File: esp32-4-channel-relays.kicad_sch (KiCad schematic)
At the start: 27 parts, among them Q1 MBT3904DW1, SW1 SW_SKQG, SW2 SW_SKQG, U1 AMS1117-3.3, U2 CH340C, U3 PRTR5V0U2X, U4 ESP32-WROOM-32

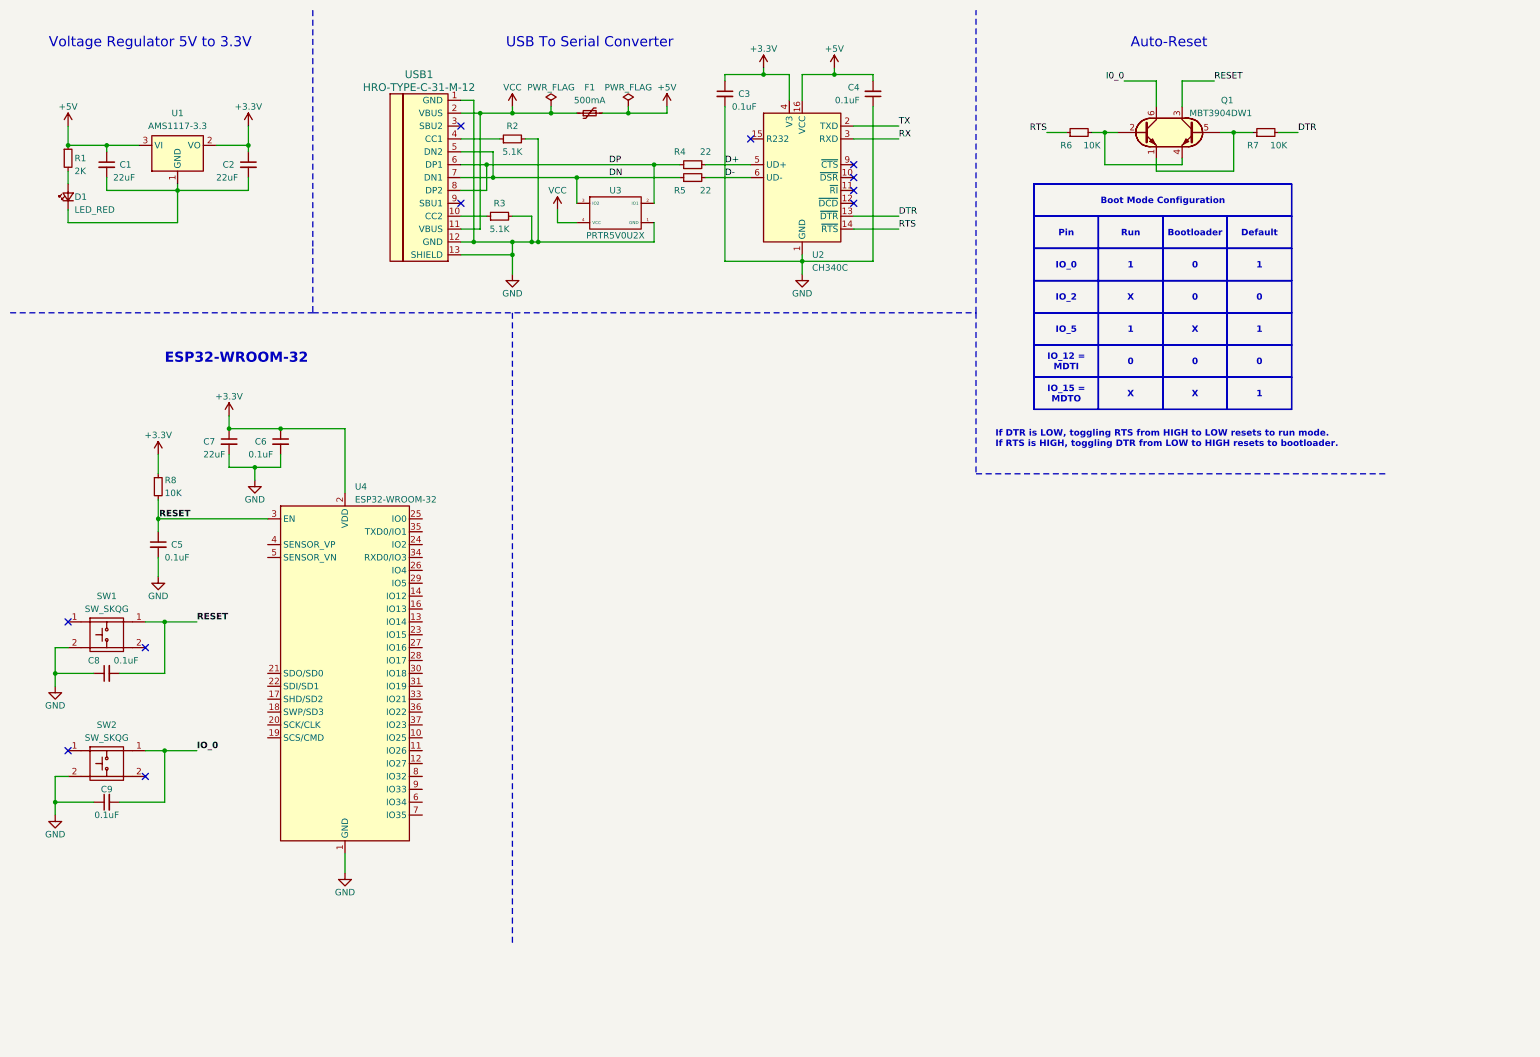
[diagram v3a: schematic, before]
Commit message: Add 4-channel relays to the schematic
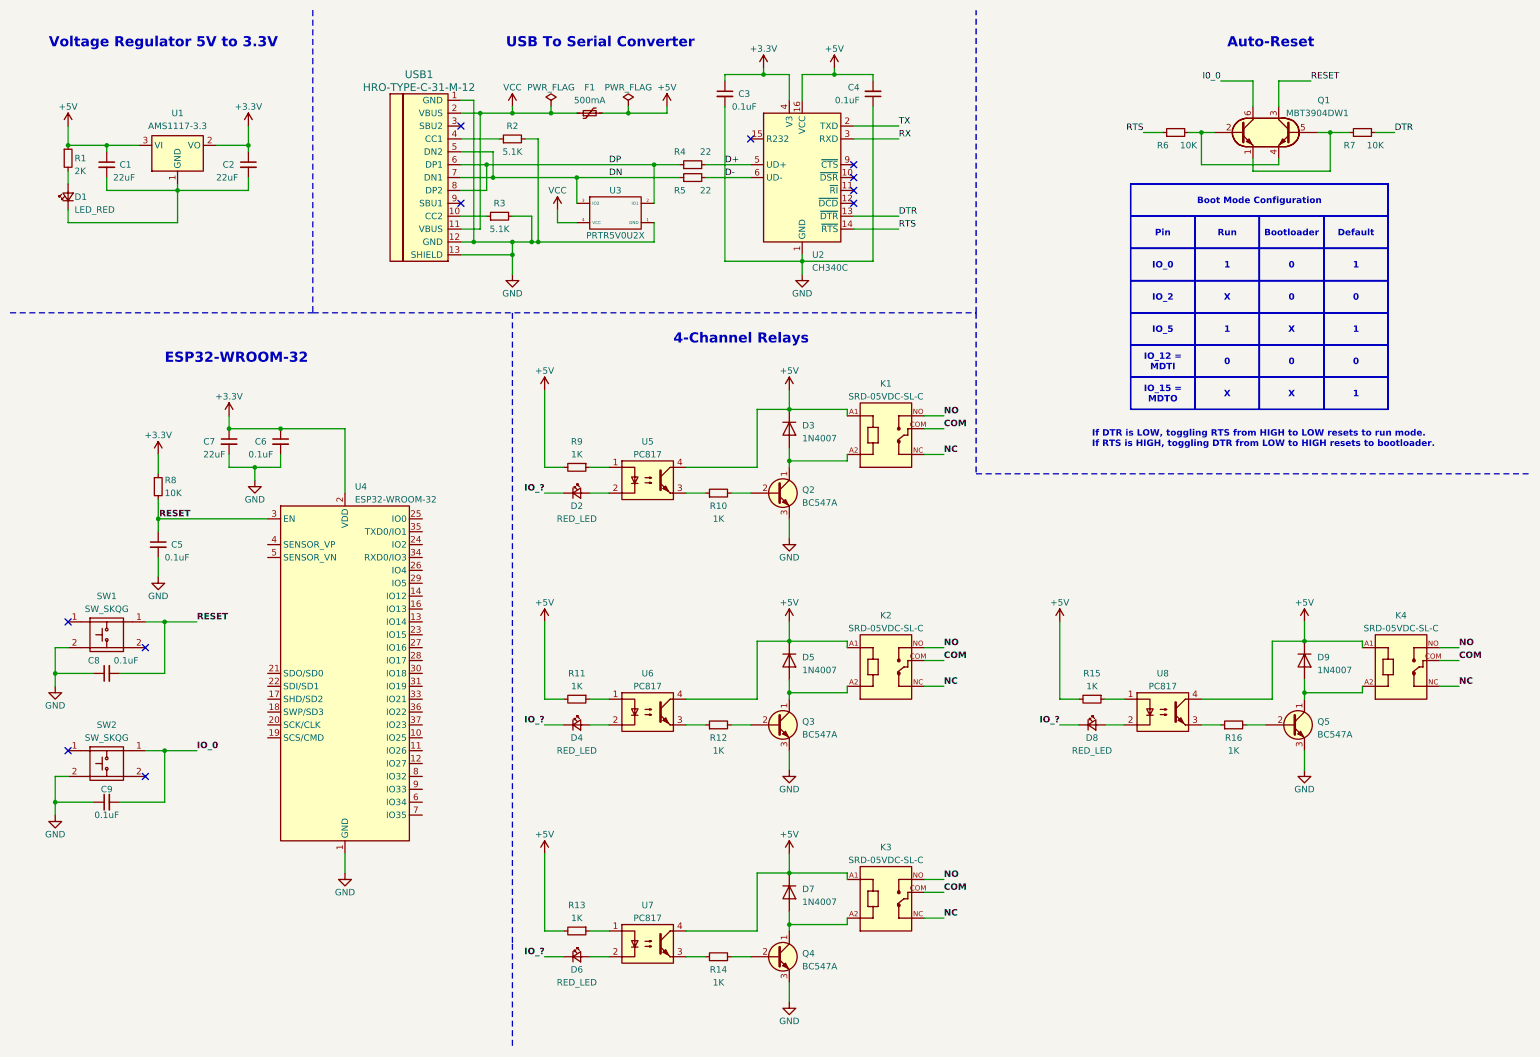
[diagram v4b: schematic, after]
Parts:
- added D2, D4, D6, D8: RED_LED, symbol Device:LED_Small
- added D3, D5, D7, D9: 1N4007, Diode_SMD:D_MELF_Handsoldering, symbol local_lib:1N4007
- added K1, K2, K3, K4: SRD-05VDC-SL-C, RELAY_SRD-05VDC-SL-C, symbol local_lib:SRD-05VDC-SL-C
- added Q2, Q3, Q4, Q5: BC547A, Package_TO_SOT_THT_AKL:TO-92_Inline_Wide_CBE, symbol local_lib:BC547A
- added R10, R11, R12, R13, R14, R15, R16, R9: 1K, symbol Device:R_Small
- added U5, U6, U7, U8: PC817, Package_DIP:DIP-4_W7.62mm, symbol local_lib:PC817
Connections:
- net +5V: now also D3.1 (K), D5.1 (K), D7.1 (K), D9.1 (K), K1.A1, K2.A1, K3.A1, K4.A1, R11.2, R13.2, R15.2, R9.2, U5.4, U6.4, U7.4, U8.4
- net GND: now also Q2.3 (E), Q3.3 (E), Q4.3 (E), Q5.3 (E)
- new net: D2.2 (A), U5.2
- new net: D4.2 (A), U6.2
- new net: R15.1, U8.1
- new net: D8.2 (A), U8.2
- new net: R16.1, U8.3
- new net: D7.2 (A), K3.A2, Q4.1 (C)
- new net: Q4.2 (B), R14.2
- new net: R13.1, U7.1
- new net: D6.2 (A), U7.2
- new net: R14.1, U7.3
- new net: R9.1, U5.1
- new net: D9.2 (A), K4.A2, Q5.1 (C)
- new net: R11.1, U6.1
- new net: D3.2 (A), K1.A2, Q2.1 (C)
- new net: Q2.2 (B), R10.2
- new net: R10.1, U5.3
- new net: Q5.2 (B), R16.2
- new net: D5.2 (A), K2.A2, Q3.1 (C)
- new net: Q3.2 (B), R12.2
- new net: R12.1, U6.3
- new net COM: K1.COM, K2.COM, K3.COM, K4.COM
- new net IO_?: D2.1 (K), D4.1 (K), D6.1 (K), D8.1 (K)
- new net NC: K1.NC, K2.NC, K3.NC, K4.NC
- new net NO: K1.NO, K2.NO, K3.NO, K4.NO
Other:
- note added: "4-Channel Relays"
- title: (none) -> ESP32 4 Channel Relays
- moved on the sheet: Q1, R6, R7

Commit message: Add screw terminal  for relay output and wiring relay input to esp32 GPIO
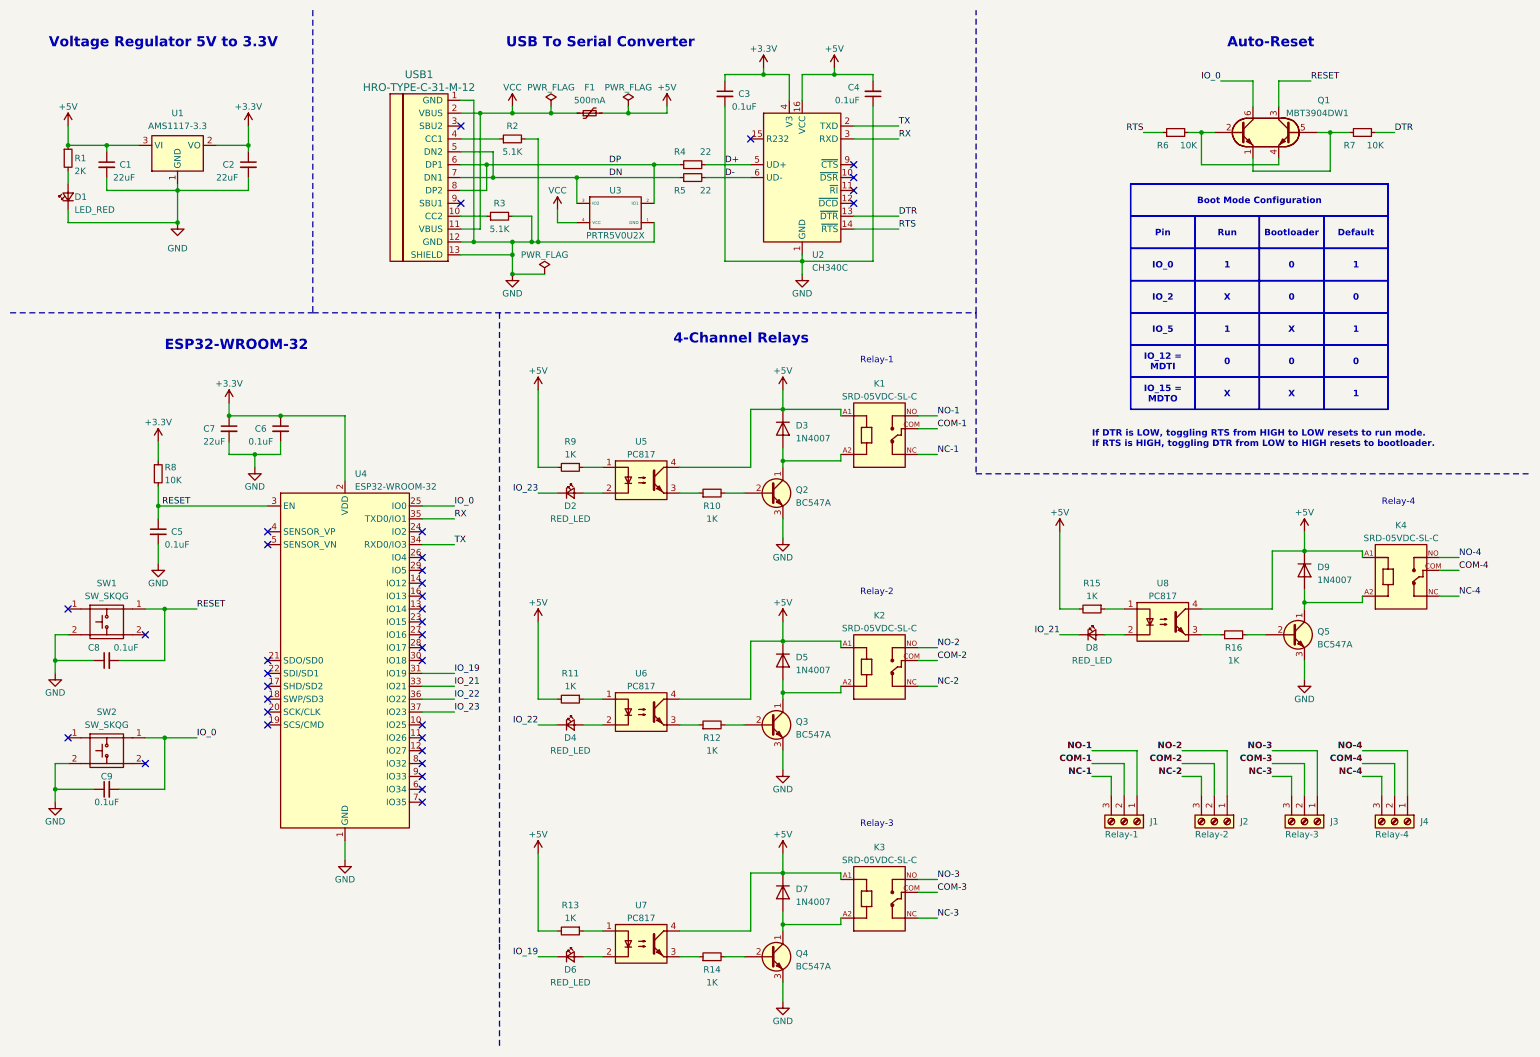
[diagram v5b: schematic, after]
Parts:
- added J1: Relay-1, symbol Connector:Screw_Terminal_01x03
- added J2: Relay-2, symbol Connector:Screw_Terminal_01x03
- added J3: Relay-3, symbol Connector:Screw_Terminal_01x03
- added J4: Relay-4, symbol Connector:Screw_Terminal_01x03
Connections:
- net I0_0 is gone; now on net IO_0: Q1.6 (C1)
- net GND: now also C1.2, C2.2, D1.1 (K), U1.1 (GND)
- net IO_0: now also U4.25 (IO0)
- net RX: now also U4.35 (TXD0/IO1)
- net TX: now also U4.34 (RXD0/IO3)
- net IO_19: now reaches U4.31 (IO19)
- net IO_19: now also D6.1 (K)
- net IO_21: now reaches U4.33 (IO21)
- net IO_21: now also D8.1 (K)
- net IO_22: now reaches U4.36 (IO22)
- net IO_22: now also D4.1 (K)
- net IO_23: now reaches U4.37 (IO23)
- net IO_23: now also D2.1 (K)
- removed net COM: K1.COM, K2.COM, K3.COM, K4.COM
- removed net IO_?: D2.1 (K), D4.1 (K), D6.1 (K), D8.1 (K)
- removed net NC: K1.NC, K2.NC, K3.NC, K4.NC
- removed net NO: K1.NO, K2.NO, K3.NO, K4.NO
- new net COM-1: J1.2 (Pin_2), K1.COM
- new net COM-2: J2.2 (Pin_2), K2.COM
- new net COM-3: J3.2 (Pin_2), K3.COM
- new net COM-4: J4.2 (Pin_2), K4.COM
- new net NC-1: J1.3 (Pin_3), K1.NC
- new net NC-2: J2.3 (Pin_3), K2.NC
- new net NC-3: J3.3 (Pin_3), K3.NC
- new net NC-4: J4.3 (Pin_3), K4.NC
- new net NO-1: J1.1 (Pin_1), K1.NO
- new net NO-2: J2.1 (Pin_1), K2.NO
- new net NO-3: J3.1 (Pin_1), K3.NO
- new net NO-4: J4.1 (Pin_1), K4.NO
- no-connect marks 11 -> 36
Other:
- note added: "Relay-1"
- note added: "Relay-2"
- note added: "Relay-3"
- note added: "Relay-4"
- moved on the sheet: C5, C6, C7, C8, C9, D2, D3, D4, D5, D6, D7, D8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

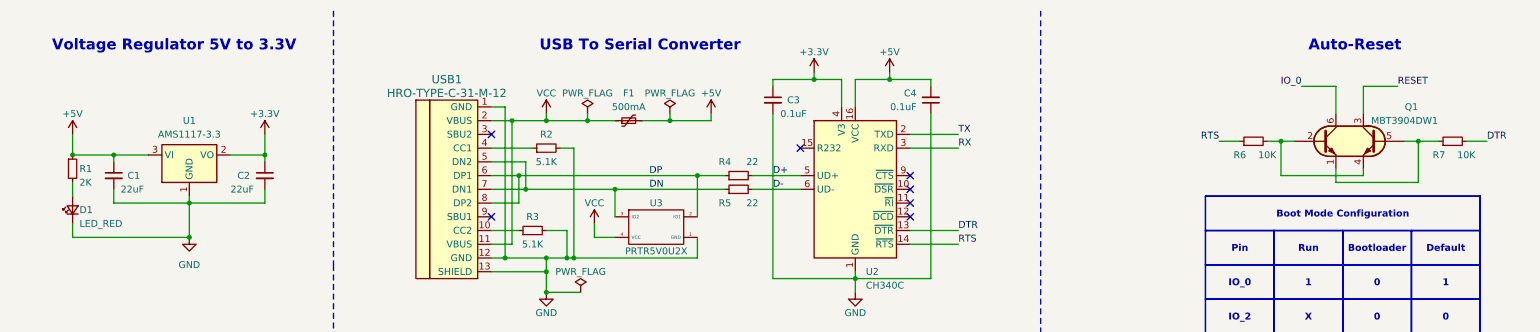
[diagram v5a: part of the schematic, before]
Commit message: Assign footprints
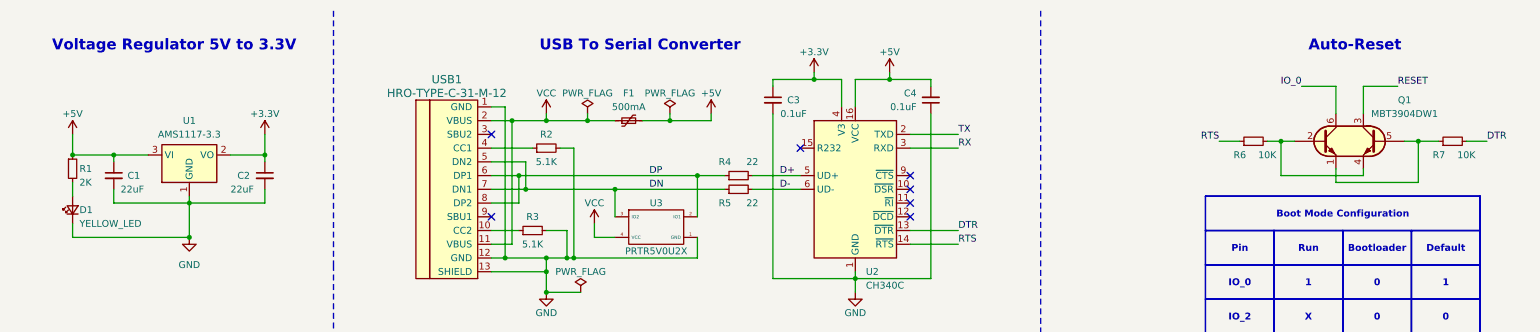
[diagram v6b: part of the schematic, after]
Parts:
- C1, C2, C3, C4, C5, C6, C7, C8, C9: footprint (none) -> Capacitor_SMD:C_0805_2012Metric_Pad1.18x1.45mm_HandSolder
- D1: value LED_RED -> YELLOW_LED; footprint (none) -> LED_SMD:LED_0805_2012Metric_Pad1.15x1.40mm_HandSolder
- D2, D4, D6, D8: footprint (none) -> LED_SMD:LED_0805_2012Metric_Pad1.15x1.40mm_HandSolder
- D3, D5, D7, D9: footprint Diode_SMD:D_MELF_Handsoldering -> local_lib:D_MELF_Handsoldering
- F1: footprint (none) -> Fuse:Fuse_1206_3216Metric_Pad1.42x1.75mm_HandSolder
- J1, J2, J3, J4: footprint (none) -> TerminalBlock_Phoenix:TerminalBlock_Phoenix_MKDS-1,5-3-5.08_1x03_P5.08mm_Horizontal
- K1, K2, K3, K4: footprint RELAY_SRD-05VDC-SL-C -> local_lib:RELAY_SRD-05VDC-SL-C
- Q1: footprint Package_TO_SOT_SMD_AKL:SOT-363_SC-70-6 -> local_lib:SOT-363_SC-70-6_Handsoldering
- Q2, Q3, Q4, Q5: footprint Package_TO_SOT_THT_AKL:TO-92_Inline_Wide_CBE -> local_lib:TSOT-23_HandSoldering
- R1, R10, R11, R12, R13, R14, R15, R16, R2, R3, R4, R5, R6, R7, R8, R9: footprint (none) -> Resistor_SMD:R_0805_2012Metric_Pad1.20x1.40mm_HandSolder
- SW1, SW2: footprint Button_Switch_SMD:SW_SPST_SKQG_WithStem -> local_lib:SW_SPST_SKQG_WithStem
- U1: footprint Package_TO_SOT_SMD:SOT-223-3_TabPin2 -> local_lib:SOT-223-3_TabPin2
- U2: footprint Package_SO:SOIC-16_3.9x9.9mm_P1.27mm -> local_lib:SOIC-16_3.9x9.9mm_P1.27mm
- U3: footprint Package_TO_SOT_SMD:SOT-143 -> local_lib:SOT-143_Handsoldering
- U4: footprint RF_Module:ESP32-WROOM-32 -> local_lib:ESP32-WROOM-32
- U5, U6, U7, U8: footprint Package_DIP:DIP-4_W7.62mm -> local_lib:SMDIP-4_W7.62mm
- USB1: footprint (none) -> local_lib:HRO-TYPE-C-31-M-12-HandSoldering
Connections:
- net GND: no longer R4.2, R5.2, U2.5 (UD+), U2.6 (UD-)
- new net D+: R4.2, U2.5 (UD+)
- new net D-: R5.2, U2.6 (UD-)

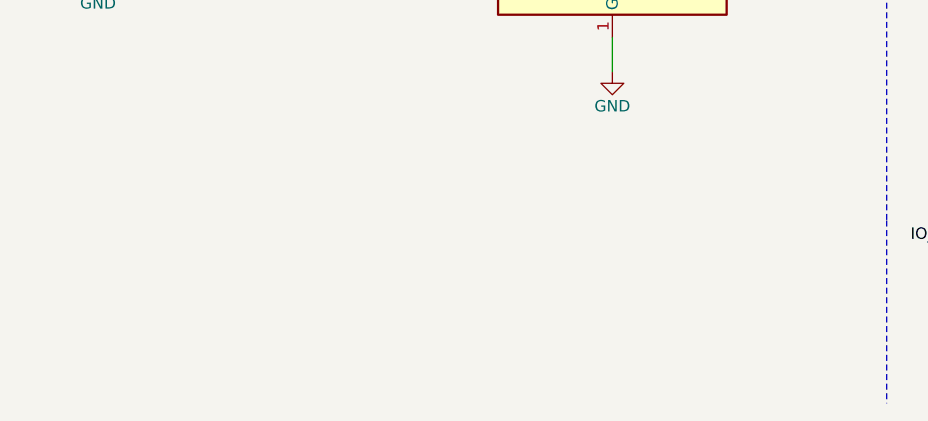
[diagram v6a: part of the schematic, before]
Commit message: Add mounting hole symbols and assign footprint
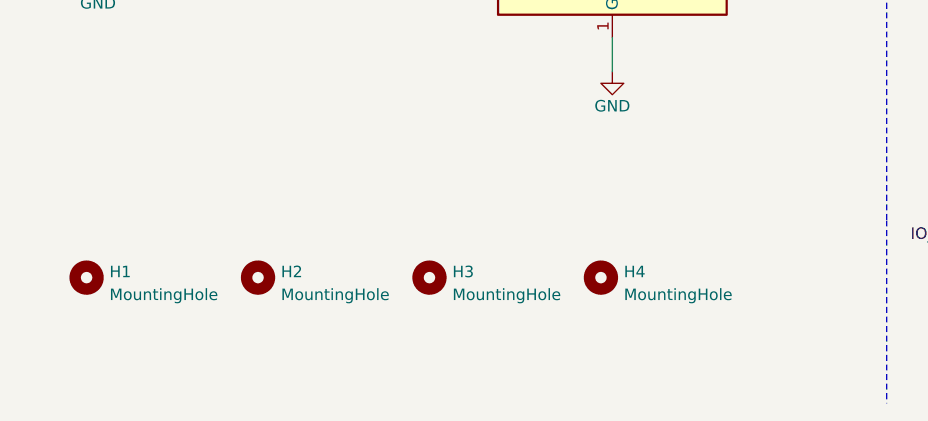
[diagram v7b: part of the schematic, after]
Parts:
- added H1, H2, H3, H4: MountingHole, MountingHole:MountingHole_3.2mm_M3, symbol Mechanical:MountingHole
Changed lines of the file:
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@@
+    )
+  )
+  (symbol (lib_id "Mechanical:MountingHole") (at 20.32 203.2 0) (unit 1)
+    (in_bom yes) (on_board yes) (dnp no) (fields_autoplaced)
+    (property "Reference" "H1" (at 22.86 202.565 0)
+      (effects (font (size 1.27 1.27)) (justify left))
+    )
+    (property "Value" "MountingHole" (at 22.86 205.105 0)
+      (effects (font (size 1.27 1.27)) (justify left))
+    )
+    (property "Footprint" "MountingHole:MountingHole_3.2mm_M3" (at 20.32 203.2 0)
+      (effects (font (size 1.27 1.27)) hide)
+    )
+    (property "Datasheet" "~" (at 20.32 203.2 0)
+      (effects (font (size 1.27 1.27)) hide)
+    )
+    (instances
+      (project "esp32-4-channel-relays"
+        (path "/8eb0840c-04b5-48e5-b6dd-a6c2b294f86f"
+          (reference "H1") (unit 1)
+        )
+      )
     )
   )
@@
     )
   )
+  (symbol (lib_id "Mechanical:MountingHole") (at 58.42 203.2 0) (unit 1)
+    (in_bom yes) (on_board yes) (dnp no) (fields_autoplaced)
+    (property "Reference" "H3" (at 60.96 202.565 0)
+      (effects (font (size 1.27 1.27)) (justify left))
+    )
+    (property "Value" "MountingHole" (at 60.96 205.105 0)
+      (effects (font (size 1.27 1.27)) (justify left))
+    )
+    (property "Footprint" "MountingHole:MountingHole_3.2mm_M3" (at 58.42 203.2 0)
+      (effects (font (size 1.27 1.27)) hide)
+    )
+    (property "Datasheet" "~" (at 58.42 203.2 0)
+      (effects (font (size 1.27 1.27)) hide)
+    )
+    (instances
+      (project "esp32-4-channel-relays"
+        (path "/8eb0840c-04b5-48e5-b6dd-a6c2b294f86f"
+          (reference "H3") (unit 1)
+        )
+      )
+    )
+  )
   (symbol (lib_id "Device:LED_Small") (at 123.19 199.39 0) (unit 1)
     (in_bom yes) (on_board yes) (dnp no)
@@
         (path "/8eb0840c-04b5-48e5-b6dd-a6c2b294f86f"
           (reference "#PWR015") (unit 1)
+        )
+      )
+    )
+  )
+  (symbol (lib_id "Mechanical:MountingHole") (at 77.47 203.2 0) (unit 1)
+    (in_bom yes) (on_board yes) (dnp no) (fields_autoplaced)
+    (property "Reference" "H4" (at 80.01 202.565 0)
+      (effects (font (size 1.27 1.27)) (justify left))
+    )
+    (property "Value" "MountingHole" (at 80.01 205.105 0)
+      (effects (font (size 1.27 1.27)) (justify left))
+    )
+    (property "Footprint" "MountingHole:MountingHole_3.2mm_M3" (at 77.47 203.2 0)
+      (effects (font (size 1.27 1.27)) hide)
+    )
+    (property "Datasheet" "~" (at 77.47 203.2 0)
+      (effects (font (size 1.27 1.27)) hide)
+    )
+    (instances
+      (project "esp32-4-channel-relays"
+        (path "/8eb0840c-04b5-48e5-b6dd-a6c2b294f86f"
+          (reference "H4") (unit 1)
         )
       )
@@
         )
       )
+    )
+  )
+  (symbol (lib_id "Mechanical:MountingHole") (at 39.37 203.2 0) (unit 1)
+    (in_bom yes) (on_board yes) (dnp no) (fields_autoplaced)
+    (property "Reference" "H2" (at 41.91 202.565 0)
+      (effects (font (size 1.27 1.27)) (justify left))
+    )
+    (property "Value" "MountingHole" (at 41.91 205.105 0)
+      (effects (font (size 1.27 1.27)) (justify left))
+    )
+    (property "Footprint" "MountingHole:MountingHole_3.2mm_M3" (at 39.37 203.2 0)
+      (effects (font (size 1.27 1.27)) hide)
+    )
+    (property "Datasheet" "~" (at 39.37 203.2 0)
+      (effects (font (size 1.27 1.27)) hide)
+    )
+    (instances
+      (project "esp32-4-channel-relays"
+        (path "/8eb0840c-04b5-48e5-b6dd-a6c2b294f86f"
+          (reference "H2") (unit 1)
+        )
+      )
